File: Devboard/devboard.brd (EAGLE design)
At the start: 100 x 69.8 mm, 116 parts, among them J1 USB-MICROB-2, J10 MJ-2509N, J11 MJ-2509N, J12 MJ-2509N, J13 MJ-2509N, J6 USB-A-HU, J7 USB-A-HU, J8 USB-A-HU, J9 USB-A-HU, Q1 2.5A/30V/105mΩ, T1 BSS138PS, U1 PCA9634PW, U4 3.3V

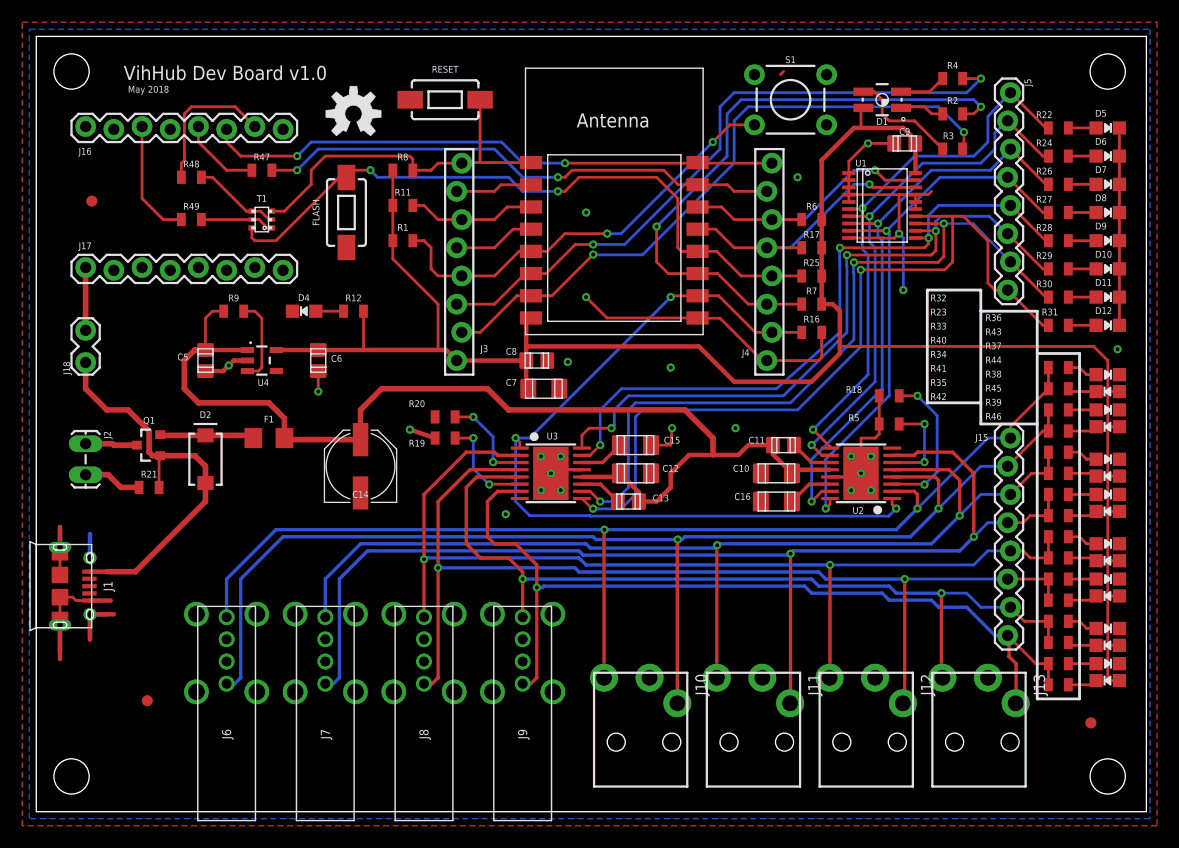
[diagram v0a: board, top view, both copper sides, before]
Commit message: Revised dev board PCB layout Added rough draft BOM
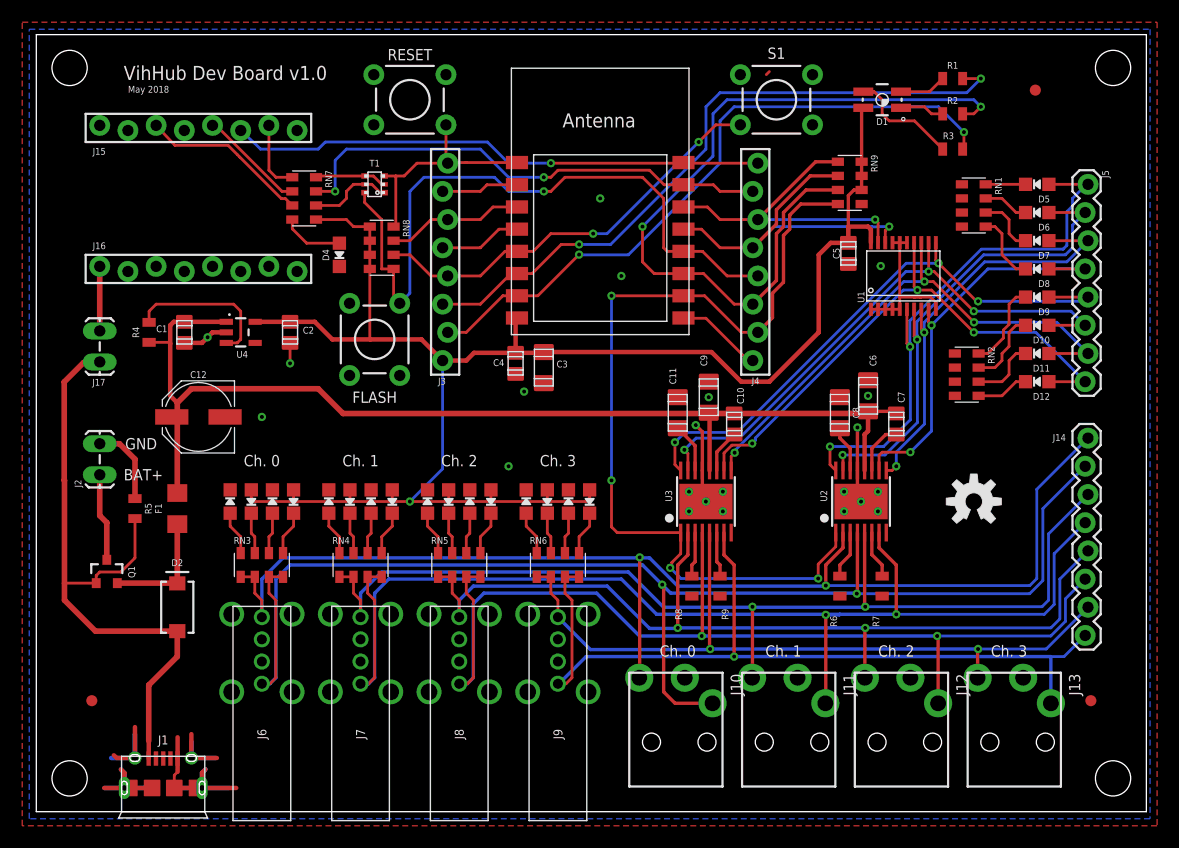
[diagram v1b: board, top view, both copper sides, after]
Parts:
- removed C13: 0.1uF/16V, vibhud:C0805
- removed C14: 10uF/25V, vibhud:PANASONIC_D
- removed C15, C16: 2.2uF/16V, vibhud:C1206
- removed J18: (no value), vibhud:1X02_LOCK
- removed R11, R16, R17, R21, R25: 10k, vibhud:0805
- removed R12, R22, R23, R24, R26, R27, R28, R29, R30, R31, R40, R41, R42, R43, R44, R45, R46: 330R, vibhud:0805
- removed R18, R19, R20: 0.43R, vibhud:0805
- removed R32, R33, R34, R35, R36, R37, R38, R39: 510R, vibhud:0805
- removed R47, R48, R49: 1k, vibhud:0805
- added C1, C2, C4: 1.0uF, vibhud:C0805
- added C3: 100uF/6.3V, vibhud:C1206
- added J14: 1x8M, vibhud:1X08_LOCK
- added RN1, RN2, RN3, RN4, RN5, RN6, RN7: 1k, vibhud:EXBS8V
- added RN8, RN9: 10k, vibhud:EXBS8V
- C10: value 10uF/16V -> 0.1uF/16V; device vibhud:C1206 -> vibhud:C0805
- C11: value 0.1uF/16V -> 2.2uF/16V; device vibhud:C0805 -> vibhud:C1206
- C12: value 10uF/16V -> 10uF/25V; device vibhud:C1206 -> vibhud:PANASONIC_D
- C5: value 1.0uF -> 10uF
- C6: value 1.0uF -> 10uF/16V; device vibhud:C0805 -> vibhud:C1206
- C7: value 100uF/6.3V -> 0.1uF/16V; device vibhud:C1206 -> vibhud:C0805
- C8: value 1.0uF -> 2.2uF/16V; device vibhud:C0805 -> vibhud:C1206
- C9: value 10uF -> 10uF/16V; device vibhud:C0805 -> vibhud:C1206
- D10, D11, D12, D21, D22, D23, D24, D25, D26, D27, D28, D4, D5, D6, D7, D8, D9: value (none) -> Blue
- D13, D14, D15, D16, D17, D18, D19, D20: value (none) -> Red
- FLASH, RESET: value MOMENTARY-SWITCH-SPST-SMD-6.0X3.5MM -> MOMENTARY-SWITCH-SPST-PTH-6.0MM; device vibhud:TACTILE_SWITCH_SMD_6.0X3.5MM -> vibhud:TACTILE_SWITCH_PTH_6.0MM
- J15, J16: value (none) -> 1x8F; device vibhud:1X08_LOCK -> vibhud:1X08_FEMALE_LOCK
- J17: value (none) -> 1x2M; device vibhud:1X08_LOCK -> vibhud:1X02_LOCK_LONGPADS
- J2: value (none) -> 1x2M
- J3, J4: value (none) -> 1x8F
- J5: value (none) -> 1x8M
- R1: value 10k -> 51R
- R4: value 51R -> 10k
- R5: value 0.43R -> 10k
- R6, R7, R8, R9: value 10k -> 0.43R
- U2, U3: value (none) -> DRV8833C
- X1: value (none) -> ESP12
- moved J15 86.5 mm to (5.71, 61.6), turned to 0 degrees
- moved FD3 85.6 mm to (90.0, 65.0)
- moved D13 79.9 mm to (17.5, 27.9), turned to 0 degrees
- moved D21 77.8 mm to (19.4, 27.9), turned to 180 degrees
- moved R4 75.9 mm to (10.2, 43.2), turned to 90 degrees
- moved D14 75.7 mm to (21.3, 27.9), turned to 0 degrees
- moved D22 73.7 mm to (23.2, 27.9), turned to 180 degrees
- moved D15 70.3 mm to (26.4, 27.9), turned to 0 degrees
- moved R5 68.4 mm to (8.89, 27.3), turned to 270 degrees
- moved D23 68.3 mm to (28.3, 27.9), turned to 180 degrees
- moved D16 66.4 mm to (30.2, 27.9), turned to 0 degrees
- moved LOGO1 65.9 mm to (84.5, 27.9)
- moved D24 64.5 mm to (32.1, 27.9), turned to 180 degrees
- moved D17 61.4 mm to (35.2, 27.9), turned to 0 degrees
- moved D25 59.6 mm to (37.1, 27.9), turned to 180 degrees
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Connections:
- removed net N$12: D10.A, R29.2
- removed net N$13: D11.A, R30.2
- removed net N$14: D12.A, R31.2
- new net N$2: D5.C, RN1.8
- new net N$3: D6.C, RN1.7
- new net N$8: D9.C, RN2.8
- net 3.3V: now also C2.1, C3.1, C4.1, C5.1, RN7.5, RN8.1, RN8.2, RN8.3, RN8.4, RN9.6, RN9.7, RN9.8; no longer C6.1, C7.1, C8.1, C9.1, R1.2, R11.2, R12.2, R17.1, R25.2, R6.1, R7.2, R8.2
- net 5V: now also C1.1, C10.1, C12.+, C6.2, C7.1, C9.2, R4.1; no longer C10.2, C11.1, C12.2, C13.1, C14.+, C5.1, R9.1
- net A_ISENSE0: now also R6.2; no longer R18.2
- net A_ISENSE1: now also R8.2; no longer R20.2
- net B_ISENSE0: now also R7.2; no longer R5.2
- net B_ISENSE1: now also R9.2; no longer R19.2
- net CH_PD: now also RN8.7; no longer R11.1
- net CP3V3: now also J16.2; no longer J17.2
- net CTS: now also J15.8; no longer J16.8
- net DCD: now also J15.2; no longer J16.2
- net DSR: now also J15.4; no longer J16.4
- net DTR: now also RN7.6; no longer R49.2
- net GND: now also C1.2, C11.1, C12.-, C2.2, C3.2, C4.2, C6.1, C8.1, C9.1, FLASH.3, J16.3, R6.1, R7.1, R8.1, R9.1, RESET.3, RN1.1, RN1.2, RN1.3, RN1.4, RN2.1, RN2.2, RN2.3, RN2.4, RN9.5; no longer C10.1, C12.1, C14.-, C15.1, C16.1, C6.2, C7.2, C8.2, C9.2, D10.C, D11.C, D12.C, D5.C, D6.C, D7.C, D8.C, D9.C, FLASH.1, J17.3, R16.2, R18.1, R19.1, R20.1, R21.1, RESET.2
- net GPIO0: now also FLASH.1, RN8.5; no longer FLASH.2, R25.1
- net GPIO12: now also R1.2; no longer R4.2
- net GPIO14: now also RN8.6; no longer R1.1
- net GPIO15: now also RN9.4; no longer R16.1
- net GPIO2: now also RN9.3; no longer R7.1
- net IO2: now also J16.6; no longer J17.6
- net IO3: now also J16.5; no longer J17.5
- net LED_G: now also R1.1; no longer R4.1
- net MOT_0N: now also J14.2, RN3.3, RN3.4; no longer J15.2, R33.1, R40.1
- net MOT_0P: now also J14.1, RN3.1, RN3.2; no longer J15.1, R23.1, R32.1
- net MOT_1N: now also J14.4, RN4.3, RN4.4; no longer J15.4, R35.1, R42.1
- net MOT_1P: now also J14.3, RN4.1, RN4.2; no longer J15.3, R34.1, R41.1
- net MOT_2N: now also J14.6, RN5.3, RN5.4; no longer J15.6, R37.1, R44.1
- net MOT_2P: now also J14.5, RN5.1, RN5.2; no longer J15.5, R36.1, R43.1
- net MOT_3N: now also J14.8, RN6.3, RN6.4; no longer J15.8, R39.1, R46.1
- net MOT_3P: now also J14.7, RN6.1, RN6.2; no longer J15.7, R38.1, R45.1
- net N$1: now also R4.2; no longer R9.2
- net N$10: now also D11.C, RN2.6; no longer D8.A, R27.2
- net N$11: now also D12.C, RN2.5; no longer D9.A, R28.2
- net N$15: now also RN3.7; no longer R23.2
- net N$16: now also RN3.8; no longer R32.2
- net N$17: now also RN3.6; no longer R33.2
- net N$18: now also RN4.8; no longer R34.2
- net N$19: now also RN4.6; no longer R35.2
- net N$20: now also RN5.8; no longer R36.2
- net N$21: now also RN5.6; no longer R37.2
- net N$22: now also RN6.8; no longer R38.2
- net N$23: now also RN6.6; no longer R39.2
- net N$24: now also RN3.5; no longer R40.2
- net N$25: now also RN4.7; no longer R41.2
- net N$26: now also RN4.5; no longer R42.2
- net N$27: now also RN6.5; no longer R46.2
- net N$28: now also RN6.7; no longer R45.2
- net N$29: now also RN5.5; no longer R44.2
- net N$30: now also RN5.7; no longer R43.2
- net N$31: now also J16.1, J17.2; no longer J17.1, J18.2
- net N$6: now also D7.C, RN1.6; no longer D5.A, R22.2
- net N$7: now also D8.C, RN1.5; no longer D6.A, R24.2
- net N$9: now also D10.C, RN2.7; no longer D7.A, R26.2
- net PWM0: now also D5.A, U2.P$16; no longer R22.1, U2.P$9
- net PWM1: now also D6.A, U2.P$15; no longer R24.1, U2.P$10
- net PWM2: now also D7.A, U2.P$9; no longer R26.1, U2.P$15
- net PWM3: now also D8.A, U2.P$10; no longer R27.1, U2.P$16
- net PWM4: now also D9.A, U3.P$16; no longer R28.1, U3.P$15
- net PWM5: now also D10.A, U3.P$15; no longer R29.1, U3.P$16
- net PWM6: now also D11.A, U3.P$9; no longer R30.1, U3.P$10
- net PWM7: now also D12.A, U3.P$10; no longer R31.1, U3.P$9
- net PWR_LED: now also RN7.4; no longer R12.1
- net RESET: now also RN8.8; no longer R8.1
- net RI: now also J15.1; no longer J16.1
- net RST: now also J16.4; no longer J17.4
- net RTS: now also RN7.8; no longer R48.2
- net RXD0: now also RN7.7; no longer R47.2
- net SCL: now also RN9.2; no longer R17.2
- net SDA: now also RN9.1; no longer R6.2
- net SU: now also J16.8; no longer J17.8
- net SU#: now also J16.7; no longer J17.7
- net TXD0: now also J15.6; no longer J16.6
- net USB_DTR: now also J15.3, RN7.3; no longer J16.3, R49.1
- net USB_RTS: now also J15.7, RN7.1; no longer J16.7, R48.1
- net USB_RXD: now also J15.5, RN7.2; no longer J16.5, R47.1
- net VCP0: now also C7.2; no longer C11.2
- net VCP1: now also C10.2; no longer C13.2
- net VINT0: now also C8.2; no longer C16.2
- net VINT1: now also C11.2; no longer C15.2
- net V_USB: now also J17.1, R5.2; no longer J18.1, R21.2
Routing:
- net GND: track 154.8 -> 122.7 mm, vias 25 -> 22
- net 3.3V: track 179.5 -> 156.4 mm, vias 0 -> 1
- net V_USB: track 36.4 -> 58.7 mm
- net PWM7: track 73.5 -> 51.4 mm, vias 2 -> 3
- net PWM6: track 68.0 -> 49.9 mm
- net PWM2: track 52.0 -> 38.6 mm
- net GPIO2: track 56.2 -> 69.4 mm
- net MOT_0N: track 112.4 -> 125.6 mm
- net RESET: track 34.4 -> 21.5 mm
- net PWM3: track 49.9 -> 37.3 mm
- net MOT_3P: track 79.0 -> 68.8 mm
- net A_ISENSE0: track 14.0 -> 4.31 mm, vias 2 -> 0
- net PWM5: track 61.6 -> 52.6 mm
- net N$8: track 0.00 -> 7.82 mm
- net PWM4: track 61.5 -> 53.7 mm
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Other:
- board size 100 x 69.8 mm -> 100 x 70 mm
- board text added: "BAT+"
- board text added: "Ch. 0"
- board text added: "Ch. 1"
- board text added: "Ch. 2"
- board text added: "Ch. 3"
- board text added: "GND"

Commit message: Updated dev board, replaced some parts that are not generally available
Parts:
- C1, C2, C4, C5: device vibhud:C0805 -> vibhud:C1206
- C10, C7: value 0.1uF/16V -> 0.1uF; device vibhud:C0805 -> vibhud:C1206
- C11, C8: value 2.2uF/16V -> 2.2uF
- C13: value 10uF/25V -> 100uF/10V
- C3: value 100uF/6.3V -> 10uF
- C6, C9: value 10uF/16V -> 10uF
- U1: value PCA9634PW -> PCA9634D; device vibhud:TSSOP20 -> vibhud:SOIC127P1032X265-20
- moved J4 17.8 mm to (64.8, 58.4), turned to 270 degrees
- moved C5 8.00 mm to (75.9, 57.8), turned to 90 degrees
- moved RN1 7.47 mm to (88.4, 61.0), turned to 180 degrees
- moved RN2 5.99 mm to (87.0, 34.3), turned to 0 degrees
- moved RN9 3.82 mm to (69.7, 58.0), turned to 0 degrees
- moved R2 3.18 mm to (82.5, 59.7)
- moved R3 3.18 mm to (82.5, 62.9)
- moved C10 0.74 mm to (63.5, 34.5)
- moved U1 0.64 mm to (78.1, 48.9)
- moved C1 0.57 mm to (13.6, 42.7)
- moved C2 0.51 mm to (22.9, 42.7)
- moved C4 0.38 mm to (43.2, 40.0)
- renumbered C12 to C13
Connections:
- net GND: now also J4.8; no longer J4.1
- net GPIO0: now also J4.5; no longer J4.4
- net GPIO15: now also J4.7; no longer J4.2
- net GPIO2: now also J4.6; no longer J4.3
- net RXD0: now also J4.2; no longer J4.7
- net SCL: now also J4.4; no longer J4.5
- net SDA: now also J4.3; no longer J4.6
- net TXD0: now also J4.1; no longer J4.8
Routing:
- net GND: track 122.7 -> 114.0 mm
- net SDA: track 29.3 -> 22.7 mm
- net N$7: track 6.29 -> 12.1 mm
- net N$8: track 7.82 -> 13.5 mm
- net SCL: track 32.7 -> 27.6 mm
- net GPIO2: track 69.4 -> 65.2 mm
- net N$6: track 5.39 -> 9.34 mm
- net N$3: track 4.12 -> 7.40 mm
- net N$9: track 6.92 -> 10.1 mm
- net LED_R: track 4.05 -> 7.05 mm
- net PWM7: track 51.4 -> 54.0 mm
- net GPIO12: track 60.8 -> 58.2 mm
- net PWM6: track 49.9 -> 52.0 mm
- net PWM4: track 53.7 -> 55.8 mm, vias 3 -> 2
- net PWM5: track 52.6 -> 54.6 mm
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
